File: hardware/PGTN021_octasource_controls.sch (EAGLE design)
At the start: 81 parts

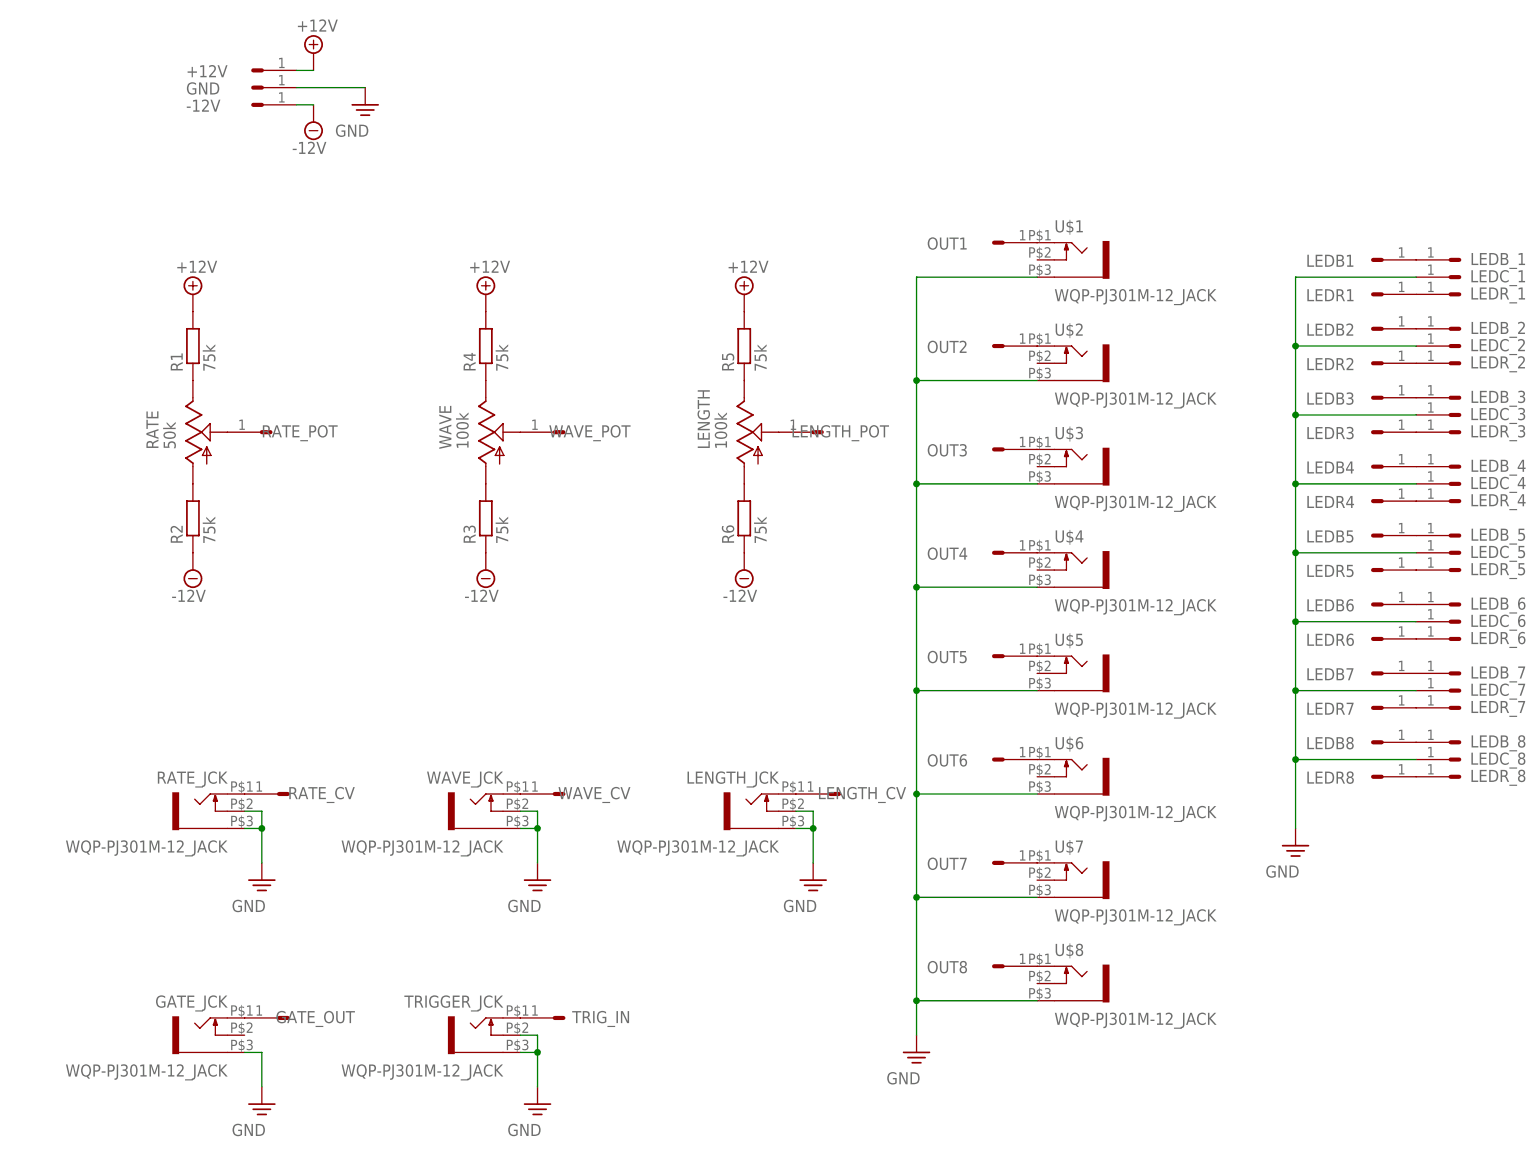
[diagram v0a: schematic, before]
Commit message: Changed resistor values to 39k
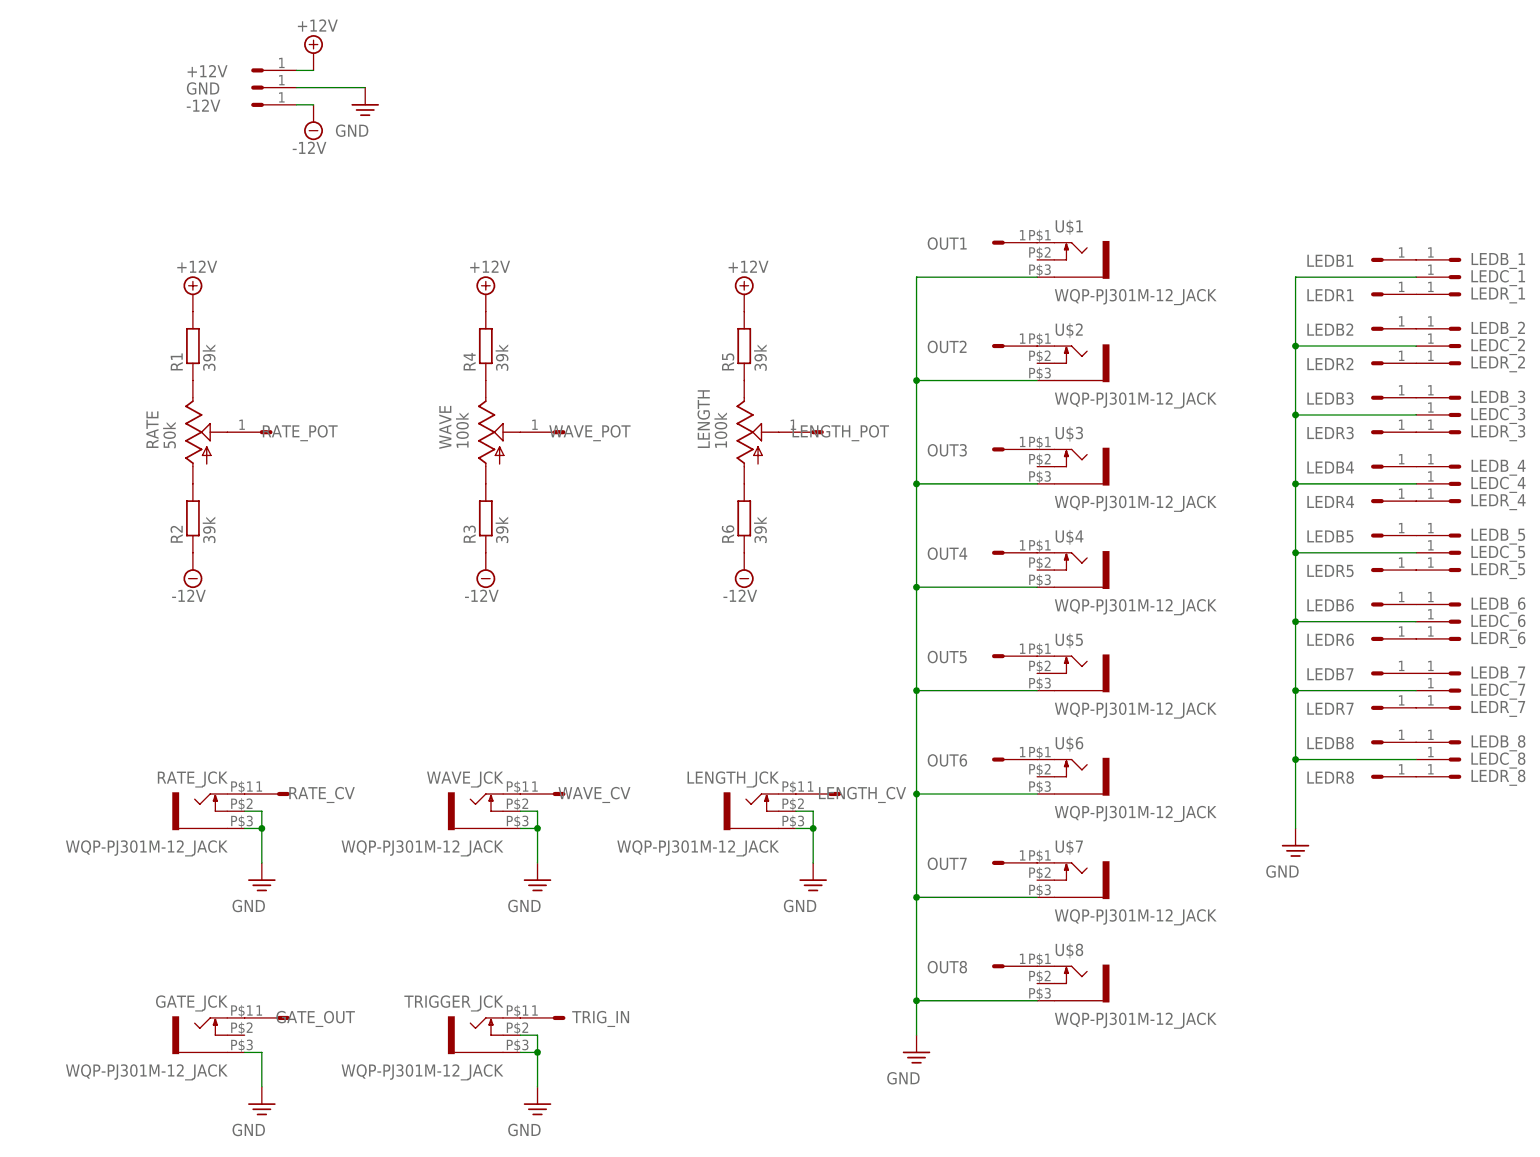
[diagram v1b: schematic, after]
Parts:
- R1, R2, R3, R4, R5, R6: value 75k -> 39k
